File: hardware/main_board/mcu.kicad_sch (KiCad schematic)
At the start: 11 parts, among them J4 Conn_02x05_Odd_Even, J5 Conn_02x10_Odd_Even, SW2 SW_Push, U4 STM32G0B1CBTx

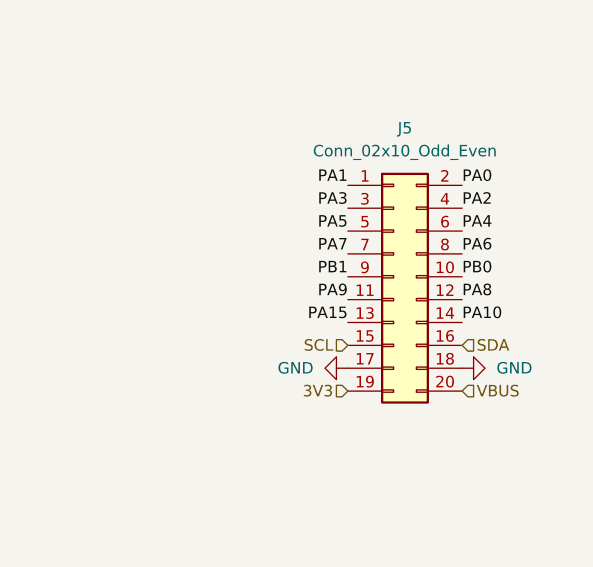
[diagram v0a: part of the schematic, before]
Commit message: Fix PCB routing errors, update LED and connector footprints
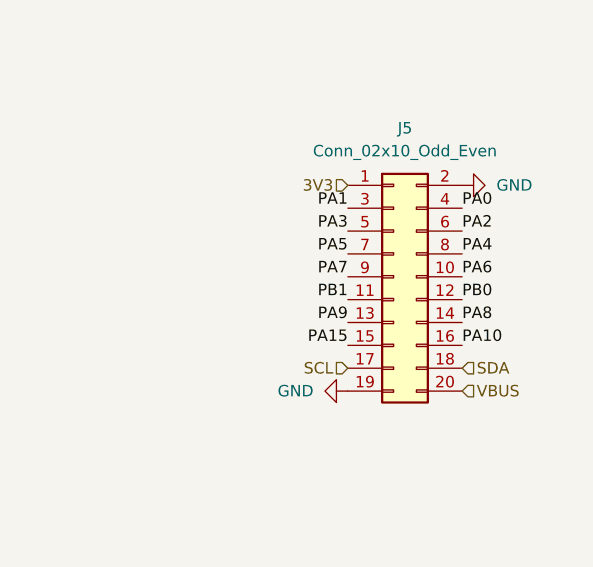
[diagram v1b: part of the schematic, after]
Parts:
- J5: footprint Project_Footprints:SAMTEC_TSM-110-01-L-DH -> Project_Footprints:SAMTEC_SSM-110-F-DH
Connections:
- net 3V3: now also J5.1 (Pin_1); no longer J5.19 (Pin_19)
- net GND: now also J5.19 (Pin_19), J5.2 (Pin_2); no longer J5.17 (Pin_17), J5.18 (Pin_18)
- net PA0: now also J5.4 (Pin_4); no longer J5.2 (Pin_2)
- net PA1: now also J5.3 (Pin_3); no longer J5.1 (Pin_1)
- net PA10: now also J5.16 (Pin_16); no longer J5.14 (Pin_14)
- net PA15: now also J5.15 (Pin_15); no longer J5.13 (Pin_13)
- net PA2: now also J5.6 (Pin_6); no longer J5.4 (Pin_4)
- net PA3: now also J5.5 (Pin_5); no longer J5.3 (Pin_3)
- net PA4: now also J5.8 (Pin_8); no longer J5.6 (Pin_6)
- net PA5: now also J5.7 (Pin_7); no longer J5.5 (Pin_5)
- net PA6: now also J5.10 (Pin_10); no longer J5.8 (Pin_8)
- net PA7: now also J5.9 (Pin_9); no longer J5.7 (Pin_7)
- net PA8: now also J5.14 (Pin_14); no longer J5.12 (Pin_12)
- net PA9: now also J5.13 (Pin_13); no longer J5.11 (Pin_11)
- net PB0: now also J5.12 (Pin_12); no longer J5.10 (Pin_10)
- net PB1: now also J5.11 (Pin_11); no longer J5.9 (Pin_9)
- net SCL: now also J5.17 (Pin_17); no longer J5.15 (Pin_15)
- net SDA: now also J5.18 (Pin_18); no longer J5.16 (Pin_16)
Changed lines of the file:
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@@
 	)
 	(label "PA0"
-		(at 243.84 82.55 0)
+		(at 243.84 85.09 0)
 		(effects
 			(font
@@
 	)
 	(label "PA8"
-		(at 243.84 95.25 0)
+		(at 243.84 97.79 0)
 		(effects
 			(font
@@
 	)
 	(label "PA4"
-		(at 243.84 87.63 0)
+		(at 243.84 90.17 0)
 		(effects
 			(font
@@
 	)
 	(label "PA1"
-		(at 231.14 82.55 180)
+		(at 231.14 85.09 180)
 		(effects
 			(font
@@
 	)
 	(label "PA2"
-		(at 243.84 85.09 0)
+		(at 243.84 87.63 0)
 		(effects
 			(font
@@
 	)
 	(label "PB0"
-		(at 243.84 92.71 0)
+		(at 243.84 95.25 0)
 		(effects
 			(font
@@
 	)
 	(label "PA5"
-		(at 231.14 87.63 180)
+		(at 231.14 90.17 180)
 		(effects
 			(font
@@
 	)
 	(label "PA6"
-		(at 243.84 90.17 0)
+		(at 243.84 92.71 0)
 		(effects
 			(font
@@
 	)
 	(label "PB1"
-		(at 231.14 92.71 180)
+		(at 231.14 95.25 180)
 		(effects
 			(font
@@
 	)
 	(label "PA15"
-		(at 231.14 97.79 180)
+		(at 231.14 100.33 180)
 		(effects
 			(font
@@
 	)
 	(label "PA10"
-		(at 243.84 97.79 0)
+		(at 243.84 100.33 0)
 		(effects
 			(font
@@
 	)
 	(label "PA7"
-		(at 231.14 90.17 180)
+		(at 231.14 92.71 180)
 		(effects
 			(font
@@
 	)
 	(label "PA3"
-		(at 231.14 85.09 180)
+		(at 231.14 87.63 180)
 		(effects
 			(font
@@
 	)
 	(label "PA9"
-		(at 231.14 95.25 180)
+		(at 231.14 97.79 180)
 		(effects
 			(font
@@
 	(hierarchical_label "SCL"
 		(shape input)
-		(at 231.14 100.33 180)
+		(at 231.14 102.87 180)
 		(effects
 			(font
@@
 	(hierarchical_label "SDA"
 		(shape input)
-		(at 243.84 100.33 0)
+		(at 243.84 102.87 0)
 		(effects
 			(font
@@
 	(hierarchical_label "3V3"
 		(shape input)
-		(at 231.14 105.41 180)
+		(at 231.14 82.55 180)
 		(effects
 			(font
@@
 	(symbol
 		(lib_id "power:GND")
-		(at 243.84 102.87 90)
+		(at 243.84 82.55 90)
 		(mirror x)
 		(unit 1)
@@
 		(dnp no)
 		(property "Reference" "#PWR28"
-			(at 250.19 102.87 0)
+			(at 250.19 82.55 0)
 			(effects
 				(font
@@
 		)
 		(property "Value" "GND"
-			(at 247.65 102.8699 90)
+			(at 247.65 82.5499 90)
 			(effects
 				(font
@@
 		)
 		(property "Footprint" ""
-			(at 243.84 102.87 0)
+			(at 243.84 82.55 0)
 			(effects
 				(font
@@
 		)
 		(property "Datasheet" ""
-			(at 243.84 102.87 0)
+			(at 243.84 82.55 0)
 			(effects
 				(font
@@
 		)
 		(property "Description" "Power symbol creates a global label with name \"GND\" , ground"
-			(at 243.84 102.87 0)
+			(at 243.84 82.55 0)
 			(effects
 				(font
@@
 	(symbol
 		(lib_id "power:GND")
-		(at 231.14 102.87 270)
+		(at 231.14 105.41 270)
 		(mirror x)
 		(unit 1)
@@
 		(on_board yes)
 		(dnp no)
-		(fields_autoplaced yes)
 		(property "Reference" "#PWR27"
-			(at 224.79 102.87 0)
+			(at 224.79 105.41 0)
 			(effects
 				(font
@@
 		)
 		(property "Value" "GND"
-			(at 227.33 102.8701 90)
+			(at 227.33 105.4101 90)
 			(effects
 				(font
@@
 		)
 		(property "Footprint" ""
-			(at 231.14 102.87 0)
+			(at 231.14 105.41 0)
 			(effects
 				(font
@@
 		)
 		(property "Datasheet" ""
-			(at 231.14 102.87 0)
+			(at 231.14 105.41 0)
 			(effects
 				(font
@@
 		)
 		(property "Description" "Power symbol creates a global label with name \"GND\" , ground"
-			(at 231.14 102.87 0)
+			(at 231.14 105.41 0)
 			(effects
 				(font
@@
 			)
 		)
-		(property "Footprint" "Project_Footprints:SAMTEC_TSM-110-01-L-DH"
+		(property "Footprint" "Project_Footprints:SAMTEC_SSM-110-F-DH"
 			(at 236.22 92.71 0)
 			(effects

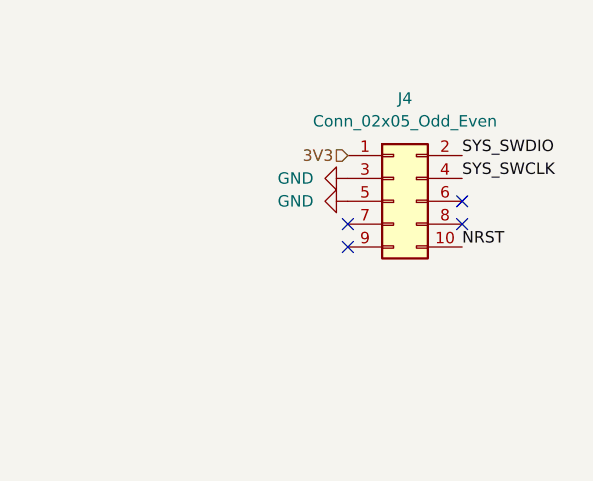
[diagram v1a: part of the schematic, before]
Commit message: Correct orientation of the debug connector
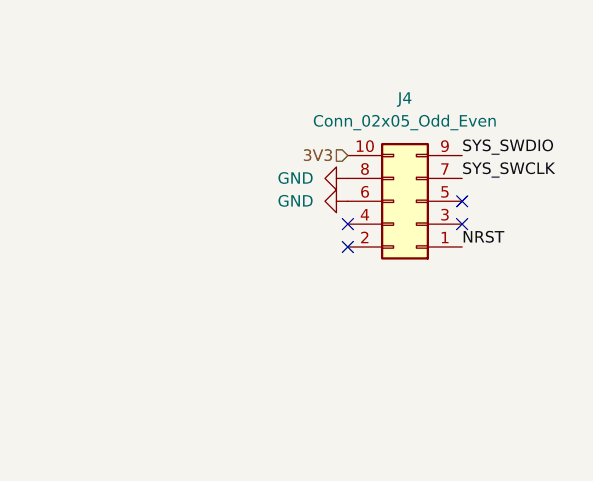
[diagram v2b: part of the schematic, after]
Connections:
- net 3V3: now also J4.10 (Pin_10); no longer J4.1 (Pin_1)
- net GND: now also J4.6 (Pin_6), J4.8 (Pin_8); no longer J4.3 (Pin_3), J4.5 (Pin_5)
- net NRST: now also J4.1 (Pin_1); no longer J4.10 (Pin_10)
- net SYS_SWCLK: now also J4.7 (Pin_7); no longer J4.4 (Pin_4)
- net SYS_SWDIO: now also J4.9 (Pin_9); no longer J4.2 (Pin_2)
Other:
- moved on the sheet: J4
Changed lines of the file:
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@@
 	(symbol
 		(lib_id "Connector_Generic:Conn_02x05_Odd_Even")
-		(at 236.22 40.64 0)
+		(at 238.76 40.64 180)
 		(unit 1)
 		(exclude_from_sim no)
@@
 		)
 		(property "Footprint" "Project_Footprints:SAMTEC_FTSH-105-01-L-D-RA-K"
-			(at 236.22 40.64 0)
+			(at 238.76 40.64 0)
 			(effects
 				(font
@@
 		)
 		(property "Datasheet" "~"
-			(at 236.22 40.64 0)
+			(at 238.76 40.64 0)
 			(effects
 				(font
@@
 		)
 		(property "Description" "Generic connector, double row, 02x05, odd/even pin numbering scheme (row 1 odd numbers, row 2 even numbers), script generated (kicad-library-utils/schlib/autogen/connector/)"
-			(at 236.22 40.64 0)
+			(at 238.76 40.64 0)
 			(effects
 				(font

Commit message: Route 4-layer PCB
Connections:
- net BUTTON: now also U4.22 (PB10); no longer U4.27 (PB15)
- net CENTER: now also U4.27 (PB15); no longer U4.25 (PB13)
- net DIR_A: now also U4.23 (PB11); no longer U4.24 (PB12)
- net DIR_B: now also U4.25 (PB13); no longer U4.23 (PB11)
- net DIR_D: now also U4.24 (PB12); no longer U4.22 (PB10)
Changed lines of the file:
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@@
 	(hierarchical_label "CENTER"
 		(shape bidirectional)
-		(at 109.22 130.81 0)
+		(at 109.22 135.89 0)
 		(effects
 			(font
@@
 	(hierarchical_label "DIR_B"
 		(shape bidirectional)
-		(at 109.22 125.73 0)
+		(at 109.22 130.81 0)
 		(effects
 			(font
@@
 	(hierarchical_label "DIR_A"
 		(shape bidirectional)
-		(at 109.22 128.27 0)
+		(at 109.22 125.73 0)
 		(effects
 			(font
@@
 	(hierarchical_label "DIR_D"
 		(shape bidirectional)
-		(at 109.22 123.19 0)
+		(at 109.22 128.27 0)
 		(effects
 			(font
@@
 	(hierarchical_label "BUTTON"
 		(shape bidirectional)
-		(at 109.22 135.89 0)
+		(at 109.22 123.19 0)
 		(effects
 			(font

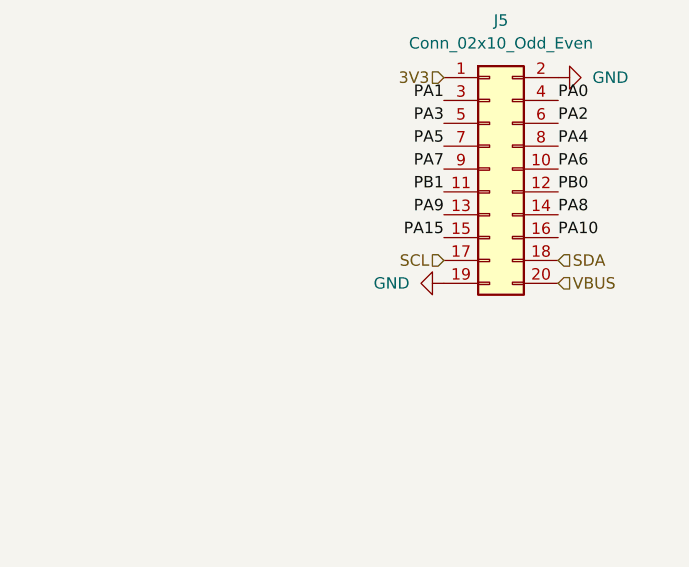
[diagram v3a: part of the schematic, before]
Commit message: Add SYS power to the extension socket
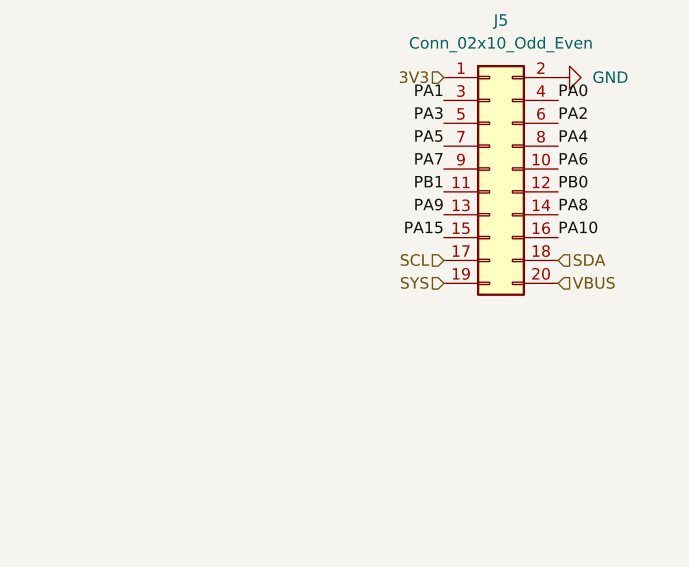
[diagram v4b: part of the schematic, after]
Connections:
- net GND: no longer J5.19 (Pin_19)
- new net SYS: J5.19 (Pin_19)
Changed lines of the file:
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@@
+		)
+	)
+	(hierarchical_label "SYS"
+		(shape input)
+		(at 231.14 105.41 180)
+		(effects
+			(font
+				(size 1.27 1.27)
+			)
+			(justify right)
 		)
 	)
@@
 					(unit 1)
 				)
-			)
-		)
-	)
-	(symbol
-		(lib_id "power:GND")
-		(at 231.14 105.41 270)
-		(mirror x)
-		(unit 1)
-		(exclude_from_sim no)
-		(in_bom yes)
-		(on_board yes)
-		(dnp no)
-		(property "Reference" "#PWR27"
-			(at 224.79 105.41 0)
-			(effects
-				(font
-					(size 1.27 1.27)
-				)
-				(hide yes)
-			)
-		)
-		(property "Value" "GND"
-			(at 227.33 105.4101 90)
-			(effects
-				(font
-					(size 1.27 1.27)
-				)
-				(justify right)
-			)
-		)
-		(property "Footprint" ""
-			(at 231.14 105.41 0)
-			(effects
-				(font
-					(size 1.27 1.27)
-				)
-				(hide yes)
-			)
-		)
-		(property "Datasheet" ""
-			(at 231.14 105.41 0)
-			(effects
-				(font
-					(size 1.27 1.27)
-				)
-				(hide yes)
-			)
-		)
-		(property "Description" "Power symbol creates a global label with name \"GND\" , ground"
-			(at 231.14 105.41 0)
-			(effects
-				(font
-					(size 1.27 1.27)
-				)
-				(hide yes)
-			)
-		)
-		(pin "1"
-		)
-		(instances
-			(project "main_board"
-				(path "/e7586151-38a0-41a9-9cce-542cfb7665db/1a2b55f4-c1fd-4586-87d2-eefd04e93091"
-					(reference "#PWR27")
-					(unit 1)
-				)
